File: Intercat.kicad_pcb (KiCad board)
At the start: 4 copper layers, 80 x 38 mm, 86 parts, among them J3 DE9_Receptacle, J4 USB_C_Receptacle_USB2.0, T1 LM-NP-1001-B1L, T4 LM-NP-1001-B1L, U1 STM32F072CBTx, U10 MAX3250, U11 EL357N(C)(TA)-G, U12 EL357N(C)(TA)-G, U2 USBLC6-2SC6, U3 PCM3060, U4 MCP6002, U5 AMS1117-3.3, U6 MCP6002, U8 EL357N(C)(TA)-G, U9 EL357N(C)(TA)-G

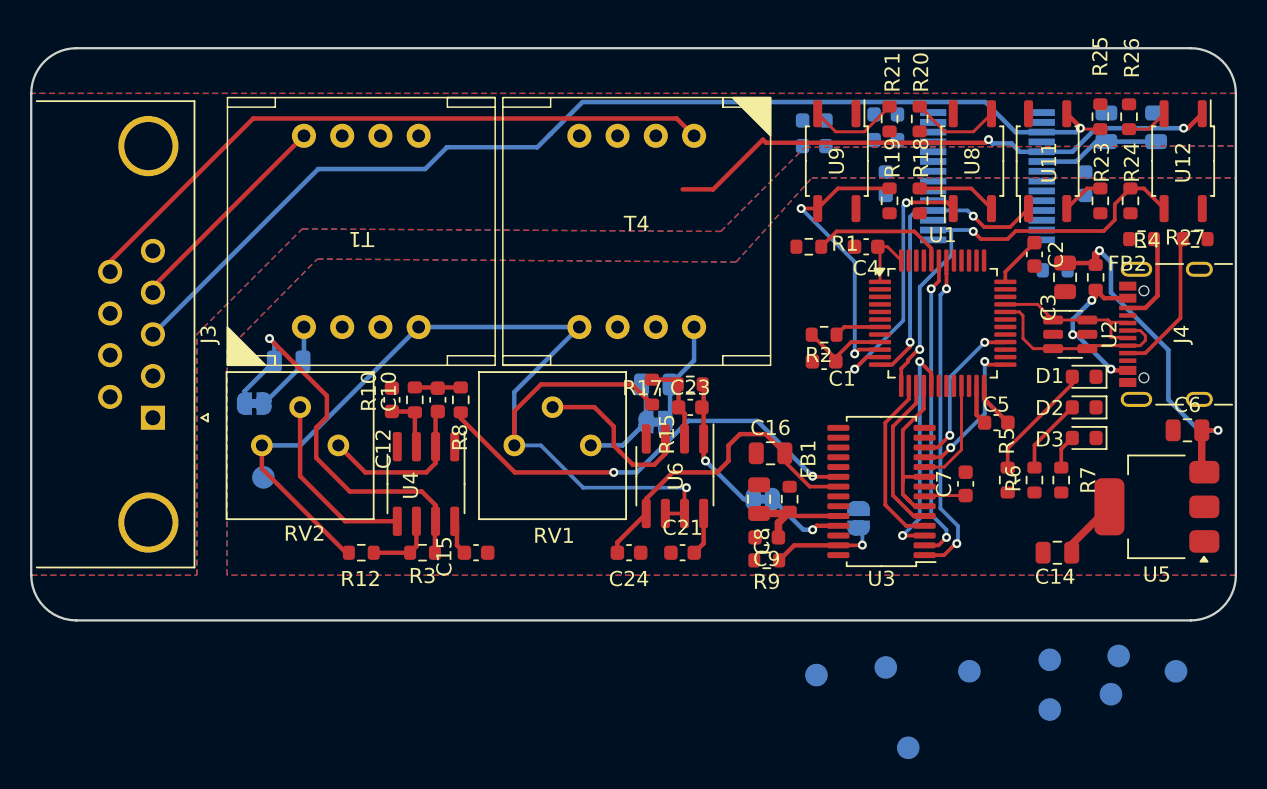
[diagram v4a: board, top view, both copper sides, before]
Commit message: First PCB version complete, to review, added 3D, changed DB9 Connecto
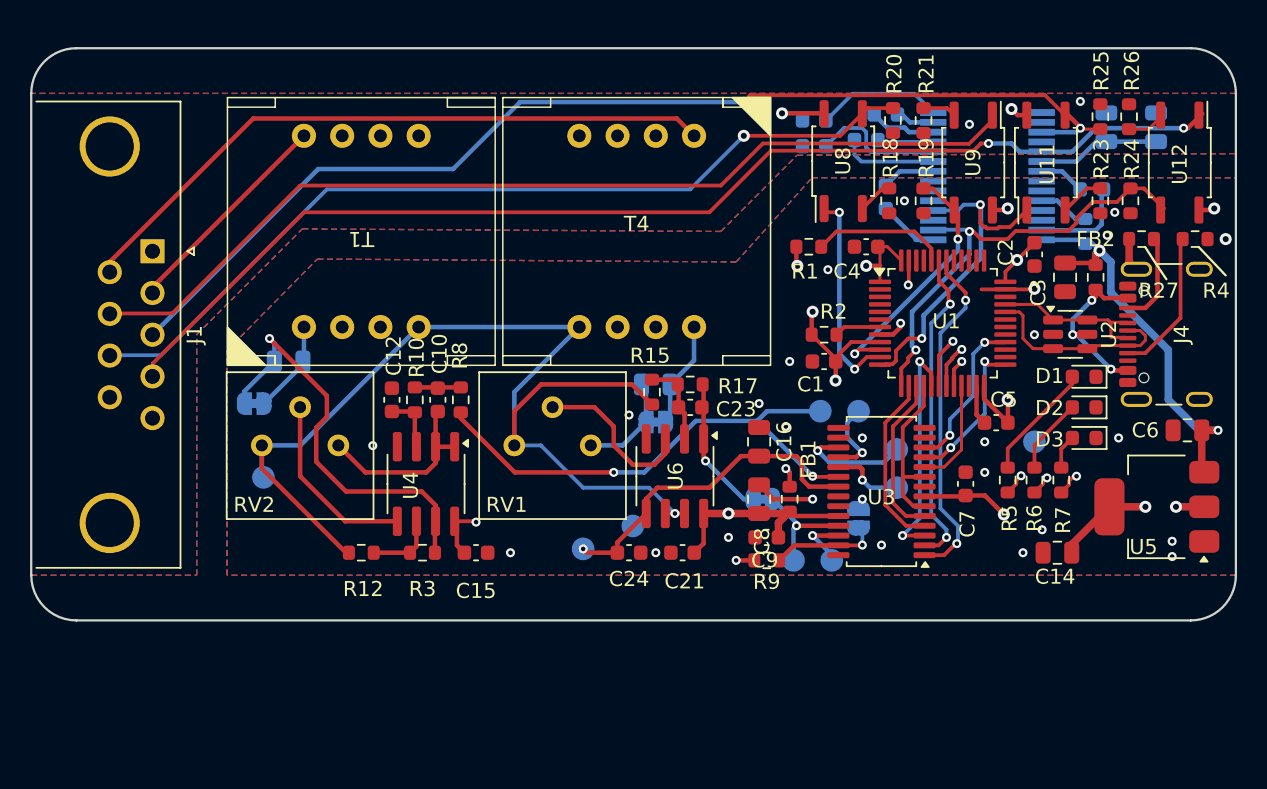
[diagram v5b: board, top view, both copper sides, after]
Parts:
- removed J3: DE9_Receptacle, Connector_Dsub:DSUB-9_Female_Horizontal_P2.77x2.84mm_EdgePinOffset4.94mm_Housed_MountingHolesOffset7.48mm
- added J1: DE9_Pins_MountingHoles, Connector_Dsub:DSUB-9_Pins_Horizontal_P2.77x2.84mm_EdgePinOffset4.94mm_Housed_MountingHolesOffset4.94mm, F.Cu at (108.1, 75.5)
- moved TP5 25.6 mm to (152.4, 86.1)
- moved TP2 25.3 mm to (136.7, 95.2)
- moved TP7 23.5 mm to (154.9, 86.1)
- moved TP6 19.8 mm to (157.5, 91.2)
- moved TP4 18.3 mm to (150.6, 96.0)
- moved TP19 17.9 mm to (166.6, 88.1)
- moved TP9 15.7 mm to (140.0, 93.7)
- moved TP8 15.5 mm to (157.5, 88.6)
- moved U9 9.06 mm to (162.6, 69.6)
- moved U8 8.58 mm to (153.9, 69.5)
- moved TP3 7.97 mm to (153.2, 96.0)
- moved R22 3.27 mm to (170.0, 74.2), turned to 90 degrees
- moved R21 2.26 mm to (159.3, 66.8)
- moved R19 2.26 mm to (159.3, 72.1)
- moved R18 2.03 mm to (157.0, 72.1)
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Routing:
- net VS: track 0.00 -> 75.5 mm, vias 0 -> 2
- net /CTS_ISO: track 0.00 -> 64.3 mm
- net /RTS_ISO: track 5.96 -> 58.8 mm, vias 0 -> 1
- net VBUS: track 23.0 -> 67.9 mm, vias 2 -> 3
- net /RX_ISO: track 37.4 -> 77.9 mm
- net +3.3V: track 23.7 -> 58.9 mm, vias 0 -> 12
- net /LED0: track 0.00 -> 20.2 mm, vias 0 -> 2
- net /LED1: track 0.00 -> 17.8 mm, vias 0 -> 2
- net /LED2: track 0.00 -> 16.0 mm, vias 0 -> 2
- net GND: track 2.66 -> 15.8 mm, vias 0 -> 28
- net Net-(U10-V+): track 0.00 -> 8.90 mm
- net Net-(U10-V-): track 0.00 -> 8.38 mm
- net Net-(U3-V_{OUT}R-): track 0.00 -> 7.40 mm, vias 0 -> 1
- net Net-(U10-C3+): track 0.00 -> 6.39 mm
- net Net-(U10-C2-): track 0.00 -> 6.08 mm
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- added copper zone on In2.Cu, net +3.3V
- added copper zone on In2.Cu, net +5V
- added copper zone on In1.Cu, net GND
- added copper zone on In1.Cu, net GNDA
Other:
- board text added: "DESIGNED BY IU2RRT"
- board text removed: "DESIGNED BY THE AMABILE IU2RRT"

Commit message: added trafo bypass, added zener reg, added todo
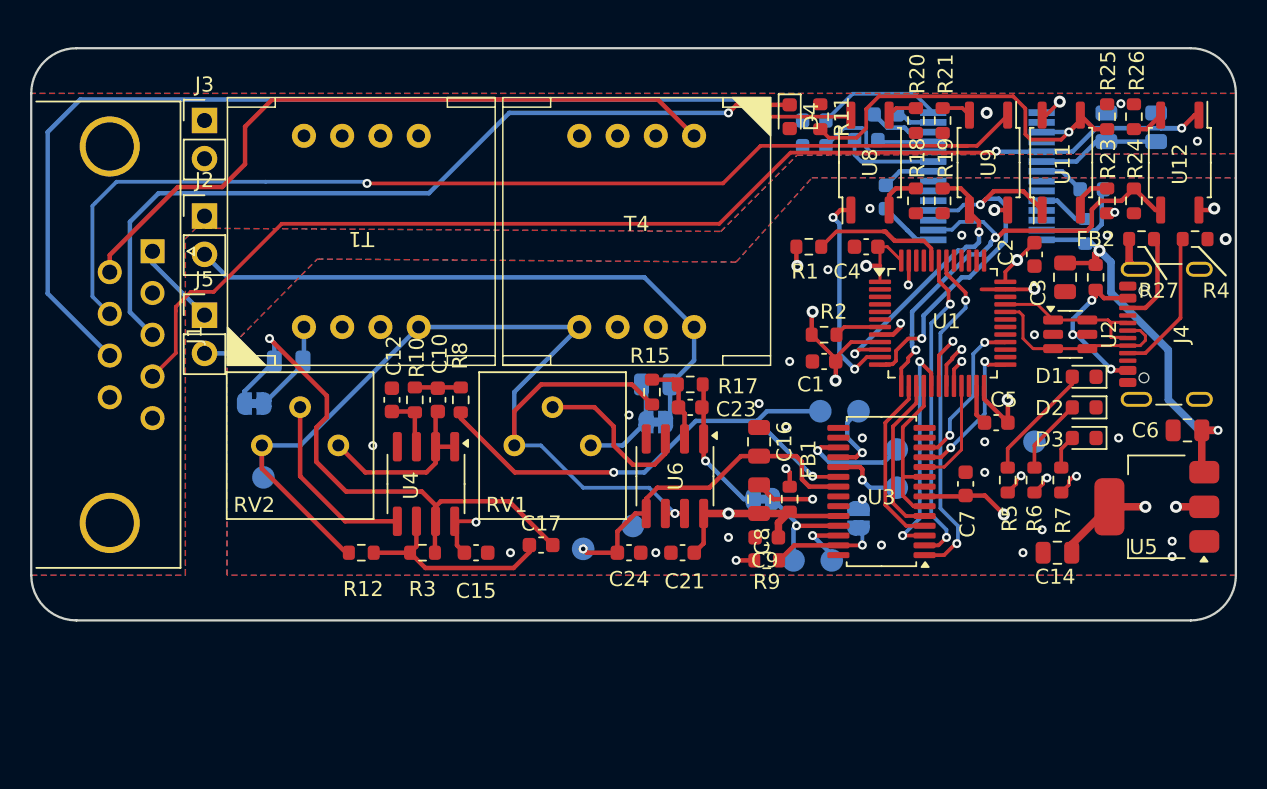
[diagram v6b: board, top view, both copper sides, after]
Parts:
- added C17: 100p, Capacitor_SMD:C_0603_1608Metric, F.Cu at (133.9, 95.0)
- added D4: 5.1V, Diode_SMD:D_0603_1608Metric, F.Cu at (150.4, 66.5)
- added J2: Conn_01x02_Pin, Connector_PinHeader_2.54mm:PinHeader_1x02_P2.54mm_Vertical, F.Cu at (111.5, 73.1)
- added J3: Conn_01x02_Pin, Connector_PinHeader_2.54mm:PinHeader_1x02_P2.54mm_Vertical, F.Cu at (111.5, 66.8)
- added J5: Conn_01x02_Pin, Connector_PinHeader_2.54mm:PinHeader_1x02_P2.54mm_Vertical, F.Cu at (111.5, 79.7)
- added R11: 330, Resistor_SMD:R_0603_1608Metric, F.Cu at (152.4, 66.5)
- R20: value 1k -> 0
- moved U8 1.78 mm to (155.7, 69.6)
- moved R18 1.78 mm to (158.8, 72.1)
- moved R20 1.52 mm to (158.8, 66.8)
- moved R19 1.27 mm to (160.5, 72.1)
- moved R21 1.27 mm to (160.5, 66.8)
- moved U11 1.02 mm to (168.4, 69.6)
- moved U9 1.02 mm to (163.6, 69.6)
- moved R23 0.45 mm to (171.4, 72.1)
- moved R25 0.45 mm to (171.4, 66.5)
- moved R26 0.32 mm to (173.2, 66.5)
- moved R24 0.23 mm to (173.2, 72.1)
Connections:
- net Net-(JP3-A) renamed /Analog Filter/In_F
- net Net-(JP4-B) renamed /Analog Filter/Out_F
- R20 pad 2: /RTS_ISO -> Net-(R20-Pad2)
- R25 pad 2: /TX_ISO -> /Digital Isolator/TX_ISO#
- U10 pad 17: /TX_ISO -> /Digital Isolator/TX_ISO#
- U11 pad 4: /TX_ISO -> /Digital Isolator/TX_ISO#
- U8 pad 4: /RTS_ISO -> Net-(R20-Pad2)
- U8 pad 6: VS -> /RTS_ISO
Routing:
- net /Analog Filter/In_F: track 7.09 -> 41.6 mm
- net /Digital Isolator/TX_ISO#: track 0.00 -> 27.5 mm, vias 0 -> 1
- net /TX_ISO: track 74.4 -> 55.1 mm, vias 2 -> 1
- net VS: track 75.5 -> 94.1 mm, vias 2 -> 1
- net /Analog Filter/Out_F: track 6.18 -> 20.1 mm
- net /RTS_ISO: track 58.8 -> 71.3 mm
- net /IN_ISO: track 43.9 -> 56.1 mm
- net /OUT_ISO: track 14.6 -> 26.8 mm
- net Net-(JP4-A): track 27.6 -> 37.7 mm
- net Net-(U4B--): track 4.68 -> 13.9 mm
- net /CTS_ISO: track 64.3 -> 71.6 mm, vias 0 -> 1
- net GNDA: track 0.00 -> 5.67 mm, vias 2 -> 3
- net /TX: track 22.8 -> 25.6 mm
- net GND: track 15.8 -> 18.3 mm, vias 28 -> 29
- net /RX_ISO: track 77.9 -> 80.0 mm
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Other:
- board text added: "XZ Group - info@xzgroup.net"
- board text removed: "XENOM NOT INCLUDED"

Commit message: added iso bypass, removed RS232, added Extra opto and prog connector
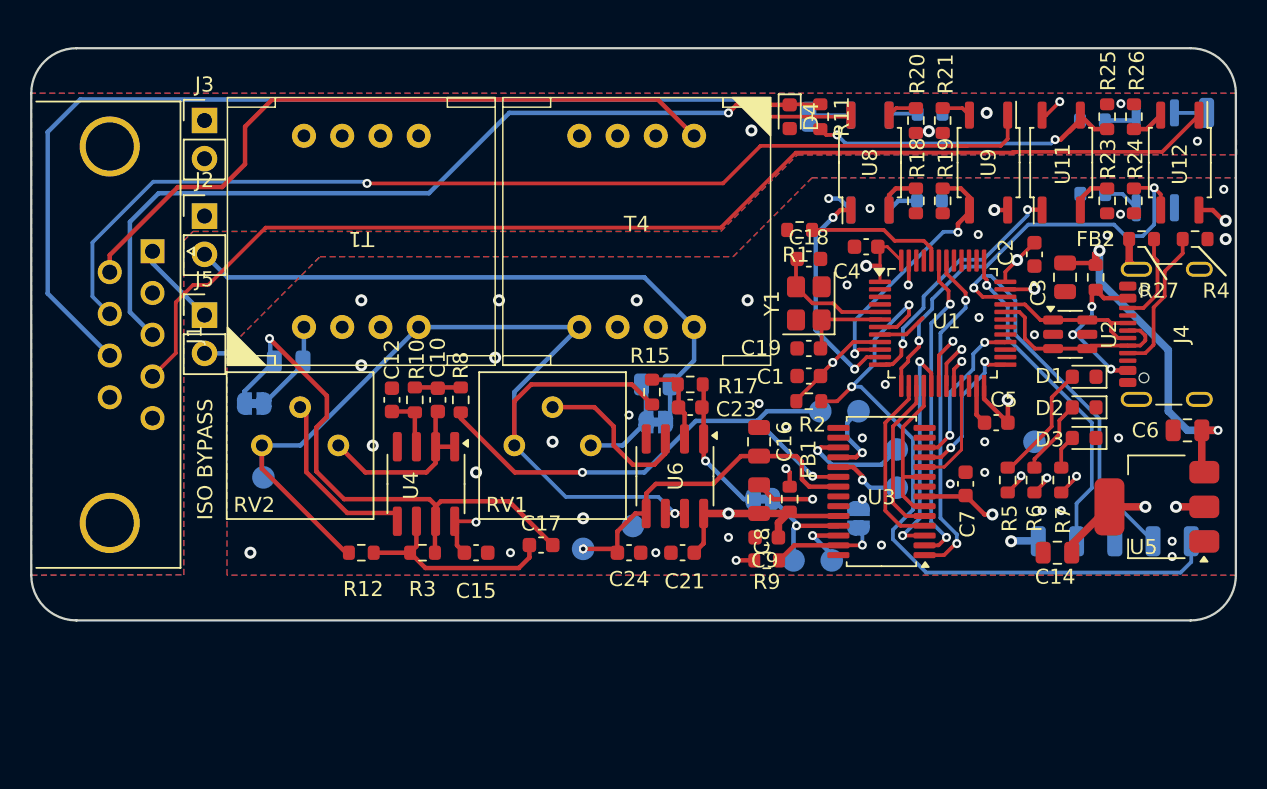
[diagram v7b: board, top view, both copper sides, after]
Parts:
- removed C25, C26, C28, C29, C31: 470n, Capacitor_SMD:C_0603_1608Metric
- removed C27, C32: 1u, Capacitor_SMD:C_0805_2012Metric
- removed C30: 100n, Capacitor_SMD:C_0603_1608Metric
- added C18: 10p, Capacitor_SMD:C_0603_1608Metric, F.Cu at (151.6, 76.0)
- added C19: 10p, Capacitor_SMD:C_0603_1608Metric, F.Cu at (151.6, 81.9)
- added J10: NRST, Connector_Wire:SolderWirePad_1x01_SMD_1x2mm, B.Cu at (177.0, 94.7)
- added J11: Conn_01x01_Pin, Connector_Wire:SolderWirePad_1x01_SMD_1x2mm, B.Cu at (178.1, 66.3)
- added J12: SWDCLK, Connector_Wire:SolderWirePad_1x01_SMD_1x2mm, B.Cu at (151.6, 66.5)
- added J6: Conn_01x01_Pin, Connector_Wire:SolderWirePad_1x01_SMD_1x2mm, B.Cu at (166.9, 94.7)
- added J7: SWDCLK, Connector_Wire:SolderWirePad_1x01_SMD_1x2mm, B.Cu at (169.4, 94.7)
- added J8: GND, Connector_Wire:SolderWirePad_1x01_SMD_1x2mm, B.Cu at (172.0, 94.7)
- added J9: SWDIO, Connector_Wire:SolderWirePad_1x01_SMD_1x2mm, B.Cu at (174.5, 94.7)
- added R13: 1k, Resistor_SMD:R_0603_1608Metric, B.Cu at (170.5, 71.7)
- added R14: 1k, Resistor_SMD:R_0603_1608Metric, B.Cu at (159.7, 72.1)
- added R16: 0, Resistor_SMD:R_0603_1608Metric, B.Cu at (170.5, 66.8)
- added U7: EL357N(C)(TA)-G, InterCat:SO-6-4_4.4x3.9mm_P2.54mm, B.Cu at (174.7, 69.4)
- added Y1: Crystal_GND24, Crystal:Crystal_SMD_3225-4Pin_3.2x2.5mm, F.Cu at (151.6, 78.9)
- U10: value MAX3250 -> EL357N(C)(TA)-G; footprint Package_SO:SSOP-28_5.3x10.2mm_P0.65mm -> InterCat:SO-6-4_4.4x3.9mm_P2.54mm
- moved R22 12.9 mm to (159.7, 66.3), turned to 180 degrees
- moved U10 7.85 mm to (155.7, 69.6), turned to -90 degrees
- moved R2 4.53 mm to (151.6, 85.4)
- moved C1 1.40 mm to (151.6, 83.8)
- moved R1 1.27 mm to (151.0, 74.1)
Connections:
- net Net-(U1-NRST) renamed /NRST
- R1 pad 2: +3.3V -> GND
- R22 pad 1: VBUS -> GNDA
- R22 pad 2: Net-(U10-nSHDN) -> Net-(R22-Pad2)
- U10 pad 1: Net-(U10-C1-) -> /DSR_ISO
- U10 pad 3: unconnected-(U10-R2OUT/N.C.-Pad3) -> Net-(R22-Pad2)
- U10 pad 4: /TX -> /DSR
- U10 pad 6: (no net) -> +3.3V
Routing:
- net /NRST: track 3.10 -> 47.5 mm, vias 0 -> 2
- net /SWDIO: track 0.00 -> 26.0 mm, vias 0 -> 1
- net /SWDCK: track 0.00 -> 22.0 mm, vias 0 -> 1
- net /TX: track 25.6 -> 16.7 mm
- net Net-(U10-V+): track 8.90 -> 0.00 mm
- net Net-(U10-V-): track 8.38 -> 0.00 mm
- net Net-(U10-ISOVCC): track 8.15 -> 0.00 mm
- net /OSCIN: track 0.00 -> 8.15 mm
- net Net-(U10-C3+): track 6.39 -> 0.00 mm
- net Net-(U10-C2-): track 6.08 -> 0.00 mm
- net /OSCOUT: track 0.00 -> 5.82 mm
- net Net-(U10-C1-): track 5.18 -> 0.00 mm
- net Net-(U10-C4+): track 4.41 -> 0.00 mm
- net Net-(U10-C1+): track 3.54 -> 0.00 mm
- net Net-(U10-C3-): track 3.50 -> 0.00 mm
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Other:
- board text added: "3v3"
- board text added: "DSR"
- board text added: "DTR"
- board text added: "ISO BYPASS"
- board text added: "NRST"
- board text added: "SWDCK"
- board text added: "SWDIO"

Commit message: added DAC_RESET and routed
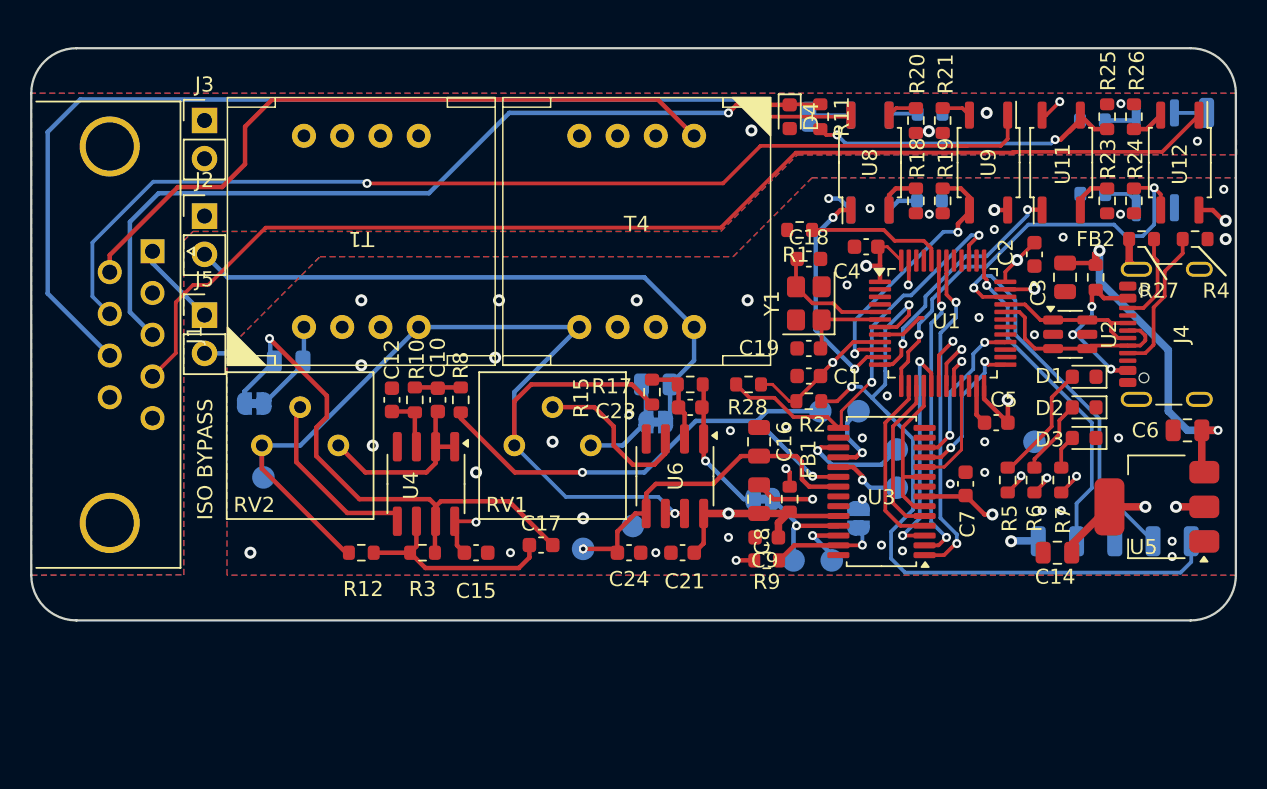
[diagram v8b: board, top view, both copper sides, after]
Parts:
- added R28: 4k7, Resistor_SMD:R_0603_1608Metric, F.Cu at (147.6, 84.3)
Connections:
- U1 pad 39: unconnected-(U1-PB3-Pad39) -> /RESET_DAC
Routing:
- net /RESET_DAC: track 0.00 -> 27.3 mm, vias 0 -> 2
- net +3.3V: track 59.9 -> 62.7 mm
- net /NRST: track 47.5 -> 49.1 mm
- net Net-(JP4-A): track 38.1 -> 37.5 mm
- net GND: vias 41 -> 43
